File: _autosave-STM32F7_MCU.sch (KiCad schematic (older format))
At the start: 49 parts, among them IC4 STM32F769IIT6, IC5 LD1117ADT33TR, Y1 25MHz, Y2 XTAL016178-85SMX

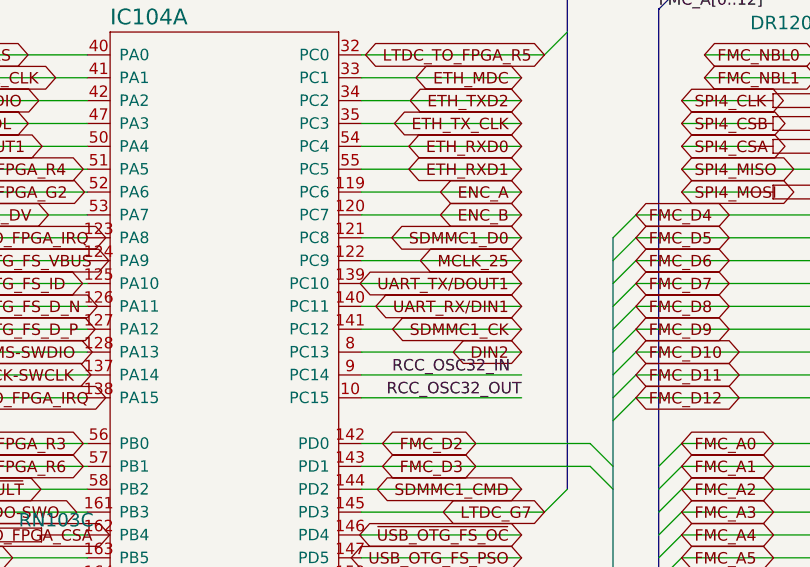
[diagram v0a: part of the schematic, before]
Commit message: Update 3D models, start to send pins to FPGA
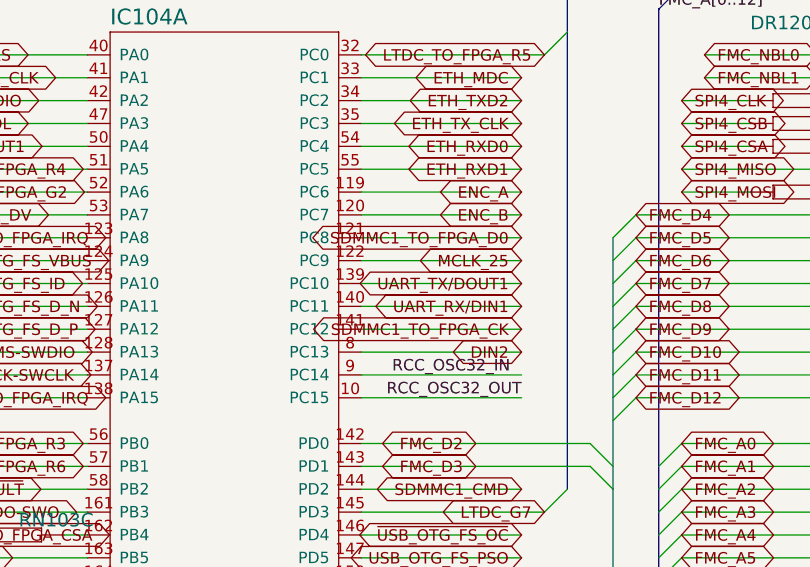
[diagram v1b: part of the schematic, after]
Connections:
- net SDMMC1_CK renamed SDMMC1_TO_FPGA_CK
- net SDMMC1_D0 renamed SDMMC1_TO_FPGA_D0
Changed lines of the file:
@@
 	3600 3400 4300 3400
 Text GLabel 4300 3400 0    50   BiDi ~ 0
-SDMMC1_D0
+SDMMC1_TO_FPGA_D0
 Wire Wire Line
 	3600 3500 4300 3500
@@
 	3600 3800 4300 3800
 Text GLabel 4300 3800 0    50   BiDi ~ 0
-SDMMC1_CK
+SDMMC1_TO_FPGA_CK
 Wire Wire Line
 	3600 3900 4300 3900
